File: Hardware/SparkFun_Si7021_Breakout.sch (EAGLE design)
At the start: 14 parts, among them U1 SI7021

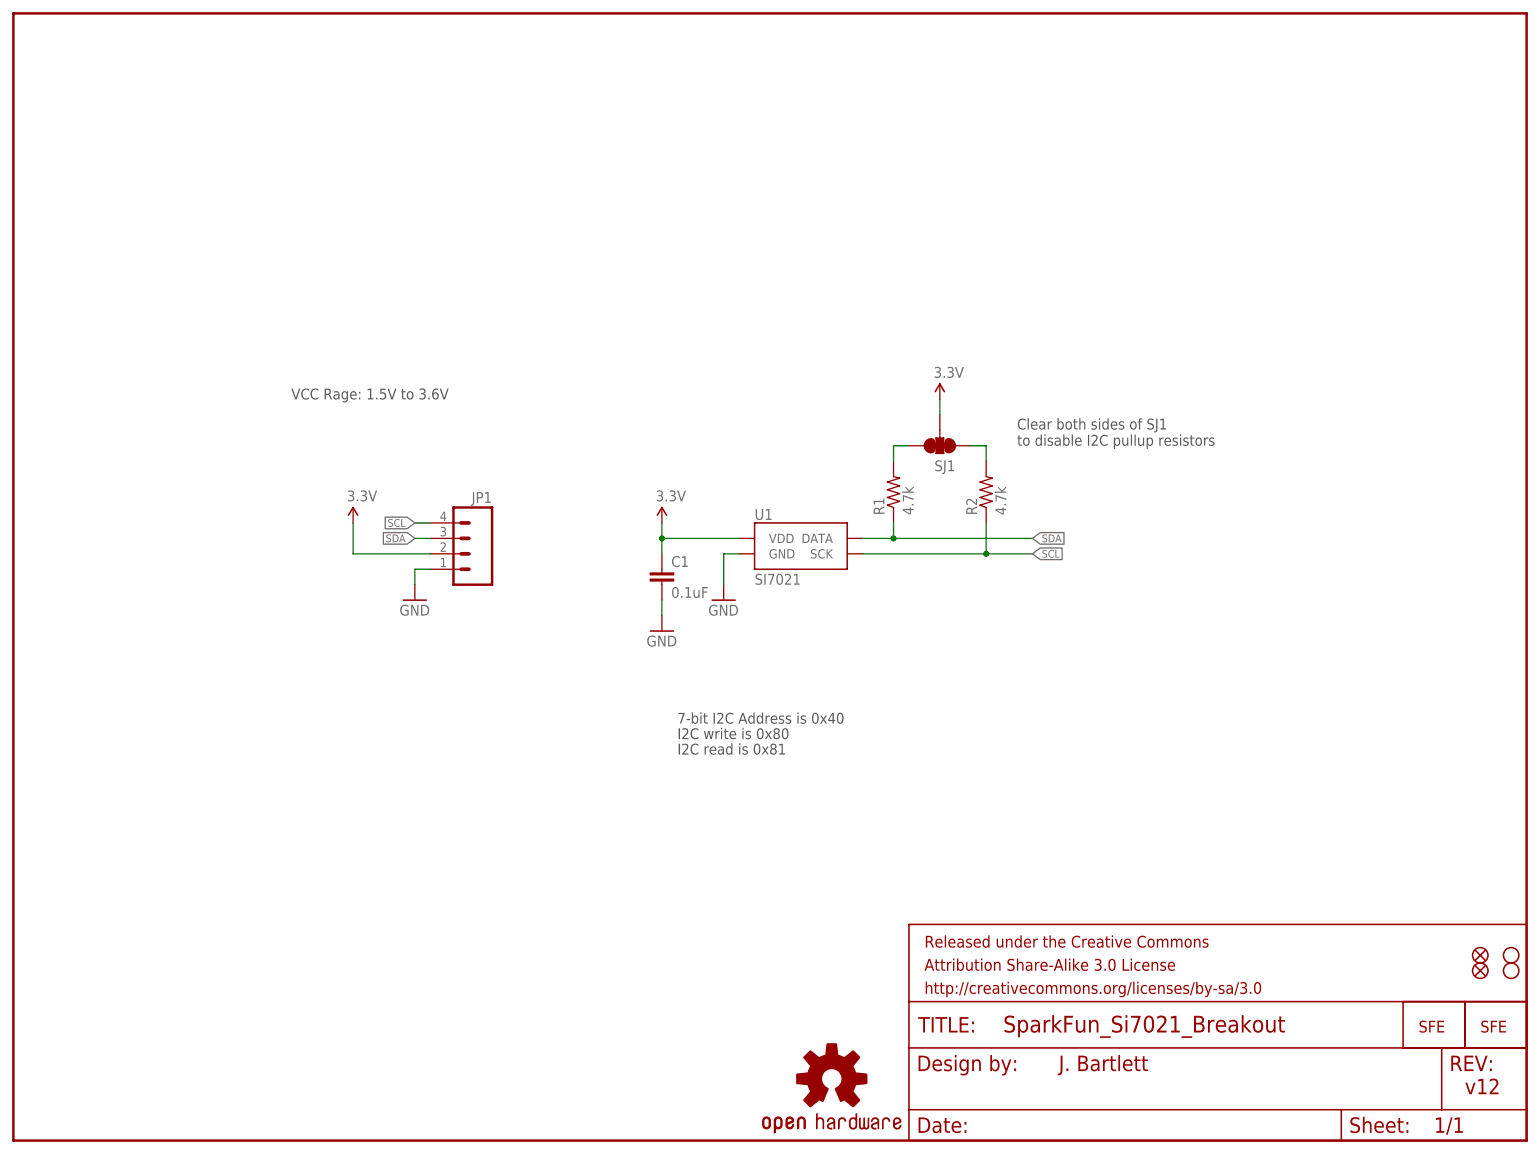
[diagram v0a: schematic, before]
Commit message: Changes from Hardware Review with Toni
Lots of minor changes brought up during Toni’s Hardware review. See
repo issues for more details.
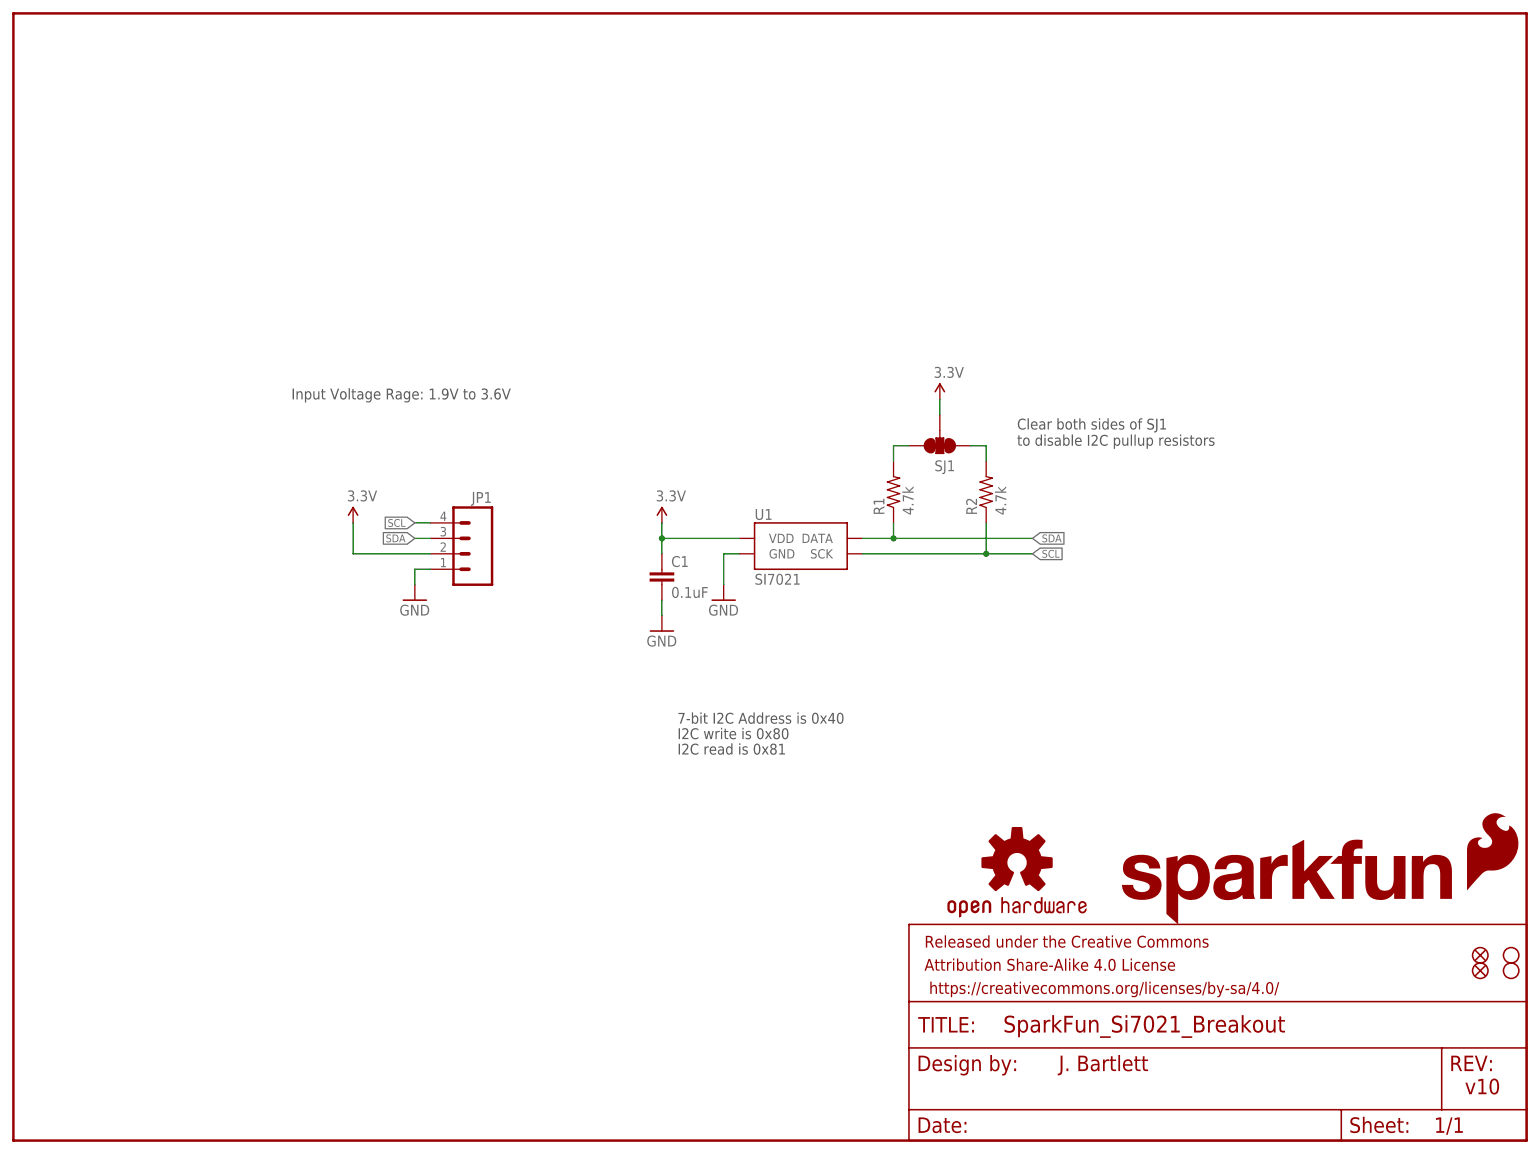
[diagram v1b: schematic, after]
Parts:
- removed JP2: LOGO-SFENW2, SparkFun-Aesthetics:LOGO-SFENW2
- removed LOGO1: LOGO-SFESK, SparkFun:LOGO-SFESK
- added LOGO3: SFE_LOGO_FLAME.1_INCH, SparkFun-Aesthetics:SFE_LOGO_FLAME.1_INCH
- added LOGO4: SFE_LOGO_NAME.1_INCH, SparkFun-Aesthetics:SFE_LOGO_NAME.1_INCH
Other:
- note added: "Input Voltage Rage: 1.9V to 3.6V"
- note added: "v10"
- note removed: "VCC Rage: 1.5V to 3.6V"
- note removed: "v12"
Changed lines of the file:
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@@
 </classes>
 <parts>
-<part name="LOGO1" library="SparkFun" deviceset="LOGO-SFE" device="SK"/>
 <part name="C1" library="SparkFun" deviceset="CAP" device="0603-CAP" value="0.1uF"/>
 <part name="R1" library="SparkFun" deviceset="RESISTOR" device="0603-RES" value="4.7k"/>
 <part name="R2" library="SparkFun" deviceset="RESISTOR" device="0603-RES" value="4.7k"/>
-<part name="GND1" library="SparkFun" deviceset="GND" device=""/>
-<part name="P+1" library="SparkFun" deviceset="VCC" device="" value="3.3V"/>
-<part name="P+3" library="SparkFun" deviceset="VCC" device="" value="3.3V"/>
 <part name="SJ1" library="mike-temp" deviceset="SOLDERJUMPER_2WAY" device="PASTE1&amp;2&amp;3"/>
-<part name="GND3" library="SparkFun" deviceset="GND" device=""/>
 <part name="STANDOFF2" library="SparkFun-Electromechanical" deviceset="STAND-OFF" device=""/>
 <part name="STANDOFF1" library="SparkFun-Electromechanical" deviceset="STAND-OFF" device=""/>
-<part name="JP2" library="SparkFun-Aesthetics" deviceset="LOGO-SFE" device="NW2"/>
 <part name="JP3" library="SparkFun-Aesthetics" deviceset="FIDUCIAL" device="UFIDUCIAL"/>
 <part name="JP4" library="SparkFun-Aesthetics" deviceset="FIDUCIAL" device="UFIDUCIAL"/>
-<part name="P+4" library="SparkFun" deviceset="VCC" device="" value="3.3V"/>
-<part name="GND4" library="SparkFun" deviceset="GND" device=""/>
 <part name="LOGO2" library="SparkFun-Aesthetics" deviceset="OSHW-LOGO" device="S"/>
 <part name="FRAME2" library="SparkFun-Aesthetics" deviceset="FRAME-LETTER" device=""/>
 <part name="JP1" library="SparkFun-Connectors" deviceset="M04" device="PTH"/>
 <part name="U1" library="SparkFun-Sensors" deviceset="SI7021" device=""/>
+<part name="LOGO3" library="SparkFun-Aesthetics" deviceset="SFE_LOGO_FLAME" device=".1_INCH"/>
+<part name="LOGO4" library="SparkFun-Aesthetics" deviceset="SFE_LOGO_NAME" device=".1_INCH"/>
+<part name="SUPPLY1" library="SparkFun-Aesthetics" deviceset="3.3V" device=""/>
+<part name="SUPPLY2" library="SparkFun-Aesthetics" deviceset="3.3V" device=""/>
+<part name="SUPPLY3" library="SparkFun-Aesthetics" deviceset="3.3V" device=""/>
+<part name="GND2" library="SparkFun-Aesthetics" deviceset="GND" device=""/>
+<part name="GND5" library="SparkFun-Aesthetics" deviceset="GND" device=""/>
+<part name="GND6" library="SparkFun-Aesthetics" deviceset="GND" device=""/>
 </parts>
 <sheets>
@@
 <text x="165.1" y="114.3" size="1.778" layer="97">Clear both sides of SJ1
 to disable I2C pullup resistors</text>
-<text x="45.72" y="121.92" size="1.778" layer="97">VCC Rage: 1.5V to 3.6V</text>
+<text x="45.72" y="121.92" size="1.778" layer="97">Input Voltage Rage: 1.9V to 3.6V</text>
 <text x="109.22" y="68.58" size="1.778" layer="97">7-bit I2C Address is 0x40</text>
 <text x="109.22" y="66.04" size="1.778" layer="97">I2C write is 0x80</text>
 <text x="109.22" y="63.5" size="1.778" layer="97">I2C read is 0x81</text>
-<text x="238.76" y="7.62" size="2.54" layer="94">v12</text>
+<text x="238.76" y="7.62" size="2.54" layer="94">v10</text>
 </plain>
 <instances>
-<instance part="LOGO1" gate="G$1" x="231.14" y="17.78"/>
 <instance part="C1" gate="G$1" x="106.68" y="91.44"/>
 <instance part="R1" gate="G$1" x="144.78" y="106.68" rot="R90"/>
 <instance part="R2" gate="G$1" x="160.02" y="106.68" rot="R90"/>
-<instance part="GND1" gate="1" x="106.68" y="83.82"/>
-<instance part="P+1" gate="1" x="106.68" y="101.6"/>
-<instance part="P+3" gate="1" x="152.4" y="121.92"/>
 <instance part="SJ1" gate="G$1" x="152.4" y="114.3" smashed="yes" rot="R270">
 <attribute name="NAME" x="154.94" y="111.887" size="1.778" layer="95" rot="R180"/>
 <attribute name="VALUE" x="150.495" y="111.76" size="1.778" layer="96" rot="R270"/>
 </instance>
-<instance part="GND3" gate="1" x="116.84" y="88.9"/>
 <instance part="STANDOFF2" gate="G$1" x="246.38" y="30.48"/>
 <instance part="STANDOFF1" gate="G$1" x="246.38" y="27.94"/>
-<instance part="JP2" gate="G$1" x="241.3" y="17.78"/>
 <instance part="JP3" gate="G$1" x="241.3" y="30.48"/>
 <instance part="JP4" gate="G$1" x="241.3" y="27.94"/>
-<instance part="P+4" gate="1" x="55.88" y="101.6"/>
-<instance part="GND4" gate="1" x="66.04" y="88.9"/>
-<instance part="LOGO2" gate="G$1" x="134.62" y="10.16"/>
+<instance part="LOGO2" gate="G$1" x="165.1" y="45.72"/>
 <instance part="FRAME2" gate="G$1" x="0" y="0"/>
-<instance part="FRAME2" gate="G$2" x="147.32" y="0"/>
+<instance part="FRAME2" gate="V" x="147.32" y="0"/>
 <instance part="JP1" gate="G$1" x="73.66" y="96.52" rot="MR0"/>
 <instance part="U1" gate="G$1" x="129.54" y="96.52"/>
+<instance part="LOGO3" gate="G$1" x="238.76" y="40.64"/>
+<instance part="LOGO4" gate="G$1" x="180.34" y="35.56"/>
+<instance part="SUPPLY1" gate="G$1" x="55.88" y="101.6"/>
+<instance part="SUPPLY2" gate="G$1" x="106.68" y="101.6"/>
+<instance part="SUPPLY3" gate="G$1" x="152.4" y="121.92"/>
+<instance part="GND2" gate="1" x="66.04" y="88.9"/>
+<instance part="GND5" gate="1" x="106.68" y="83.82"/>
+<instance part="GND6" gate="1" x="116.84" y="88.9"/>
 </instances>
 <busses>
 </busses>
 <nets>
-<net name="GND" class="0">
-<segment>
-<pinref part="GND3" gate="1" pin="GND"/>
-<wire x1="119.38" y1="96.52" x2="116.84" y2="96.52" width="0.1524" layer="91"/>
-<wire x1="116.84" y1="96.52" x2="116.84" y2="91.44" width="0.1524" layer="91"/>
-<pinref part="U1" gate="G$1" pin="GND"/>
-</segment>
-<segment>
-<wire x1="106.68" y1="86.36" x2="106.68" y2="88.9" width="0.1524" layer="91"/>
-<pinref part="GND1" gate="1" pin="GND"/>
-<pinref part="C1" gate="G$1" pin="2"/>
-</segment>
-<segment>
-<pinref part="GND4" gate="1" pin="GND"/>
-<wire x1="66.04" y1="91.44" x2="66.04" y2="93.98" width="0.1524" layer="91"/>
-<pinref part="JP1" gate="G$1" pin="1"/>
-<wire x1="66.04" y1="93.98" x2="68.58" y2="93.98" width="0.1524" layer="91"/>
-</segment>
-</net>
 <net name="SCL" class="0">
 <segment>
@@
 <net name="3.3V" class="0">
 <segment>
-<pinref part="P+1" gate="1" pin="VCC"/>
 <wire x1="119.38" y1="99.06" x2="106.68" y2="99.06" width="0.1524" layer="91"/>
 <wire x1="106.68" y1="99.06" x2="106.68" y2="101.6" width="0.1524" layer="91"/>
@@
 <pinref part="C1" gate="G$1" pin="1"/>
 <pinref part="U1" gate="G$1" pin="VDD"/>
+<pinref part="SUPPLY2" gate="G$1" pin="3.3V"/>
 </segment>
 <segment>
 <pinref part="SJ1" gate="G$1" pin="2"/>
-<pinref part="P+3" gate="1" pin="VCC"/>
 <wire x1="152.4" y1="121.92" x2="152.4" y2="119.38" width="0.1524" layer="91"/>
+<pinref part="SUPPLY3" gate="G$1" pin="3.3V"/>
 </segment>
 <segment>
-<pinref part="P+4" gate="1" pin="VCC"/>
 <pinref part="JP1" gate="G$1" pin="2"/>
 <wire x1="68.58" y1="96.52" x2="55.88" y2="96.52" width="0.1524" layer="91"/>
 <wire x1="55.88" y1="96.52" x2="55.88" y2="101.6" width="0.1524" layer="91"/>
+<pinref part="SUPPLY1" gate="G$1" pin="3.3V"/>
 </segment>
 </net>
@@
 </segment>
 </net>
+<net name="GND" class="0">
+<segment>
+<wire x1="66.04" y1="91.44" x2="66.04" y2="93.98" width="0.1524" layer="91"/>
+<pinref part="JP1" gate="G$1" pin="1"/>
+<wire x1="66.04" y1="93.98" x2="68.58" y2="93.98" width="0.1524" layer="91"/>
+<pinref part="GND2" gate="1" pin="GND"/>
+</segment>
+<segment>
+<wire x1="106.68" y1="86.36" x2="106.68" y2="88.9" width="0.1524" layer="91"/>
+<pinref part="C1" gate="G$1" pin="2"/>
+<pinref part="GND5" gate="1" pin="GND"/>
+</segment>
+<segment>
+<wire x1="119.38" y1="96.52" x2="116.84" y2="96.52" width="0.1524" layer="91"/>
+<wire x1="116.84" y1="96.52" x2="116.84" y2="91.44" width="0.1524" layer="91"/>
+<pinref part="U1" gate="G$1" pin="GND"/>
+<pinref part="GND6" gate="1" pin="GND"/>
+</segment>
+</net>

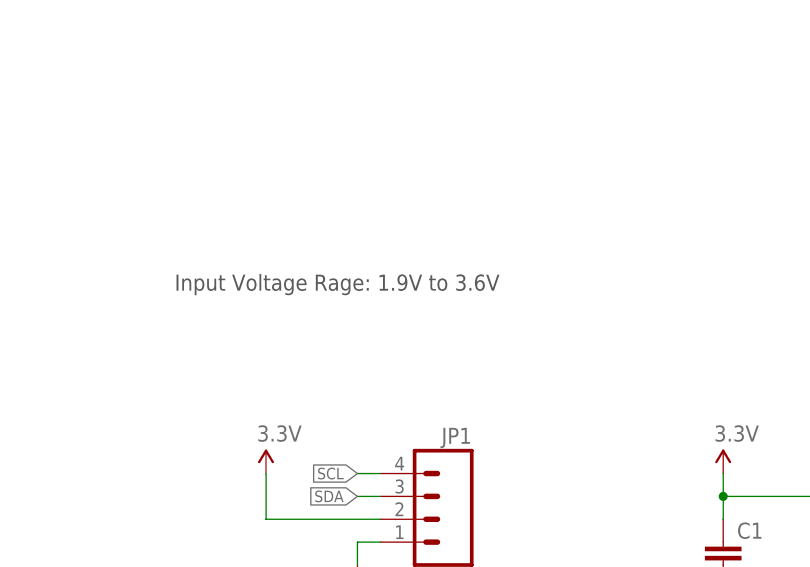
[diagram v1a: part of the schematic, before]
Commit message: Changes from Hardware Review with Marshall
very minor changes - moved via, bumped trace with up near header, minor
spelling error on sch.
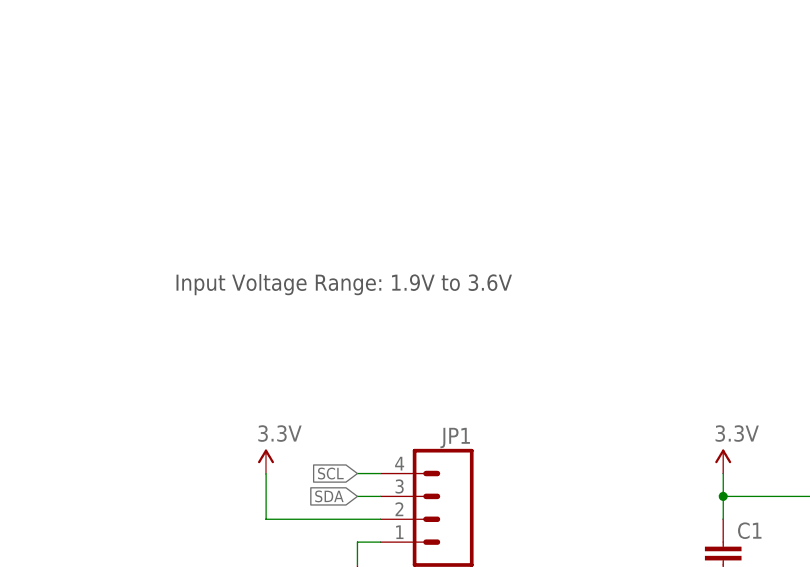
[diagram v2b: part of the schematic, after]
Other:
- note added: "Input Voltage Range: 1.9V to 3.6V"
- note removed: "Input Voltage Rage: 1.9V to 3.6V"
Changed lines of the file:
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@@
 <text x="165.1" y="114.3" size="1.778" layer="97">Clear both sides of SJ1
 to disable I2C pullup resistors</text>
-<text x="45.72" y="121.92" size="1.778" layer="97">Input Voltage Rage: 1.9V to 3.6V</text>
+<text x="45.72" y="121.92" size="1.778" layer="97">Input Voltage Range: 1.9V to 3.6V</text>
 <text x="109.22" y="68.58" size="1.778" layer="97">7-bit I2C Address is 0x40</text>
 <text x="109.22" y="66.04" size="1.778" layer="97">I2C write is 0x80</text>
